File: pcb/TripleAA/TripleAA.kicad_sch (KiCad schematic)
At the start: 5 parts, among them U1 TPS564255

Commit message: Add components
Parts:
- removed U1: TPS564255, Package_TO_SOT_SMD:SOT-563, symbol Regulator_Switching_User:TPS564255
- added C5: 100nF,50V,X7R,0603, Capacitor_SMD:C_0603_1608Metric_Pad1.08x0.95mm_HandSolder, symbol Capacitor_User:100nF,50V,X7R,0603
- added C6: 56pF,50V,C0G,0603, Capacitor_SMD:C_0603_1608Metric_Pad1.08x0.95mm_HandSolder, symbol Capacitor_User:56pF,50V,C0G,0603
- added C7: 10uF,25V,X5R,0603, Capacitor_SMD:C_0603_1608Metric_Pad1.08x0.95mm_HandSolder, symbol Capacitor_User:10uF,25V,X5R,0603
- added J2: JST_S2B-PH-SM4-x, Connector_User:JST_PH_S2B-PH-SM4-TB_1x02-1MP_P2.00mm_Horizontal, symbol Connector_User:JST_S2B-PH-SM4-x
- added L1: 74438357068, Inductor_SMD_User:L_Wurth_WE-MAPI-4030, symbol Inductor_User:74438357068
- added R1: 20k,0603, Resistor_SMD:R_0603_1608Metric_Pad0.98x0.95mm_HandSolder, symbol Resistor_User:20k,0603
- added R2: 4.7k,0603, Resistor_SMD:R_0603_1608Metric_Pad0.98x0.95mm_HandSolder, symbol Resistor_User:4.7k,0603
- added U2: TPS562242, Package_TO_SOT_SMD:SOT-563, symbol Regulator_Switching_User:TPS562242
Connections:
- net +BATT: now reaches C3.1
- net +BATT: now also C2.1, C7.1, U2.1 (VIN), U2.5 (EN)
- net GND: now reaches C3.2
- net GND: now also C1.1, C2.2, C4.1, C6.1, J2.1 (Pin_1), L1.2, R1.1
- net -Vout: now reaches C4.2
- net -Vout: now also C1.2, C7.2, J2.2 (Pin_2), R2.2, U2.3 (GND)
- new net: C5.2, L1.1, U2.2 (SW)
- new net: C6.2, R1.2, R2.1, U2.6 (FB)
- new net: C5.1, U2.4 (BST)
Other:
- note added: "Battery Charger: BQ24040DSQR"
- moved on the sheet: C1, C2, C3, C4

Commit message: Update SCH and PCB
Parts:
- removed L1: 74438357068, Inductor_SMD_User:L_Wurth_WE-MAPI-4030, symbol Inductor_User:74438357068
- added C1, C2: 10uF,25V,X5R,0603, Capacitor_SMD:C_0603_1608Metric_Pad1.08x0.95mm_HandSolder, symbol Capacitor_User:10uF,25V,X5R,0603
- added D1: 824021, Package_TO_SOT_SMD_User:SOT-23_Handsoldering, symbol Power_Protection_User:824021
- added D2: 150080GS75000, LED_SMD:LED_0805_2012Metric_Pad1.15x1.40mm_HandSolder, symbol LED_User:150080GS75000
- added D3: 150080SS75000, LED_SMD:LED_0805_2012Metric_Pad1.15x1.40mm_HandSolder, symbol LED_User:150080SS75000
- added J1: JST_S2B-PH-SM4-x, Connector_User:JST_PH_S2B-PH-SM4-TB_1x02-1MP_P2.00mm_Horizontal, symbol Connector_User:JST_S2B-PH-SM4-x
- added unit 2 of J2
- added L1: 74438356056, Inductor_SMD_User:L_Wurth_WE-MAPI-4020, symbol Inductor_User:74438356056
- added R1, R2: 2k,0603, Resistor_SMD:R_0603_1608Metric_Pad0.98x0.95mm_HandSolder, symbol Resistor_User:2k,0603
- added R5: 27.4k,0603, Resistor_SMD:R_0603_1608Metric_Pad0.98x0.95mm_HandSolder, symbol Resistor_User:27.4k,0603
- added R6: 10k,0603, Resistor_SMD:R_0603_1608Metric_Pad0.98x0.95mm_HandSolder, symbol Resistor_User:10k,0603
- added U1: MCP73831-2-OT, Package_TO_SOT_SMD:SOT-23-5, symbol Battery_Management:MCP73831-2-OT
- added U3: BD4836G-xx, Package_TO_SOT_SMD:SOT-23-5, symbol Power_Supervisor_User:BD4836G-xx
- renumbered C2 to C4, C7 to C5, C5 to C6, C6 to C7, C1 to C8, C4 to C9, R1 to R3, R2 to R4
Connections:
- net +BATT: now also C2.1, R5.1, R6.1, U1.3 (V_{BAT}), U3.2 (VDD); no longer U2.5 (EN)
- net GND: now also C1.2, C2.2, D1.3 (A), J1.2 (Pin_2), J1.MP1 (MP), J1.MP2 (MP), J2.MP1 (MP), J2.MP2 (MP), L1.2, R2.2, U1.2 (V_{SS}), U3.3 (GND)
- net at C6.2, U2.2 (SW): now also L1.1
- new net: D3.1 (K), U3.1 (VOUT)
- new net: R1.2, U1.1 (STAT)
- new net: R2.1, U1.5 (PROG)
- new net: R6.2, U2.5 (EN)
- new net: D2.1 (K), R1.1
- new net: D3.2 (A), R5.2
- new net Vin: C1.1, D1.1 (K), D2.2 (A), J1.1 (Pin_1), U1.4 (V_{DD})
- no-connect marks 0 -> 1
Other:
- note added: "3.6 V threshold voltage"
- note added: "Ireg = 1 kV / R2 = 0.5 A"
- note added: "Low Battery Warning"
- note added: "Vout = 0.1 * (1 + R3 / R4) = 4.2 V"
- moved on the sheet: C3, C4, C5, C6, C7, C8, C9, R3, R4, U2

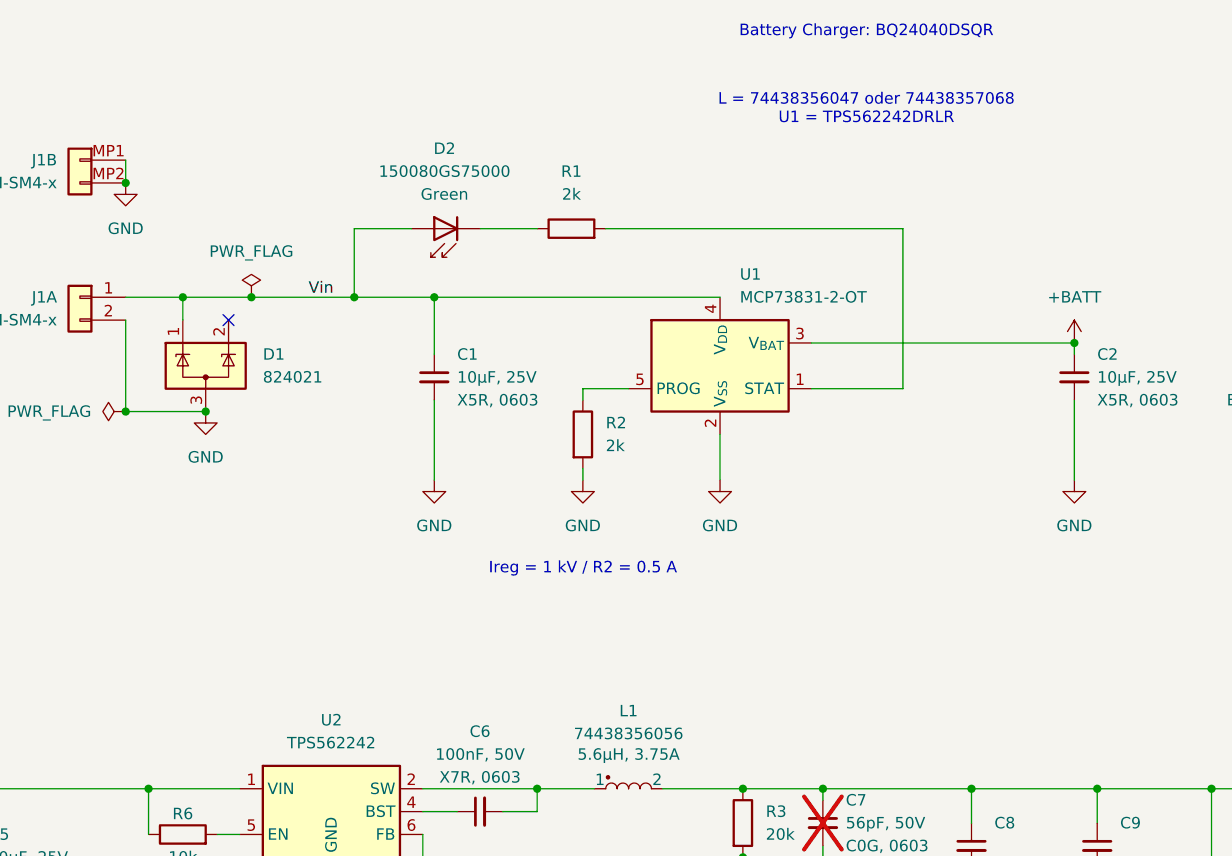
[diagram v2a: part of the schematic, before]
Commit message: Finalize PCB layout
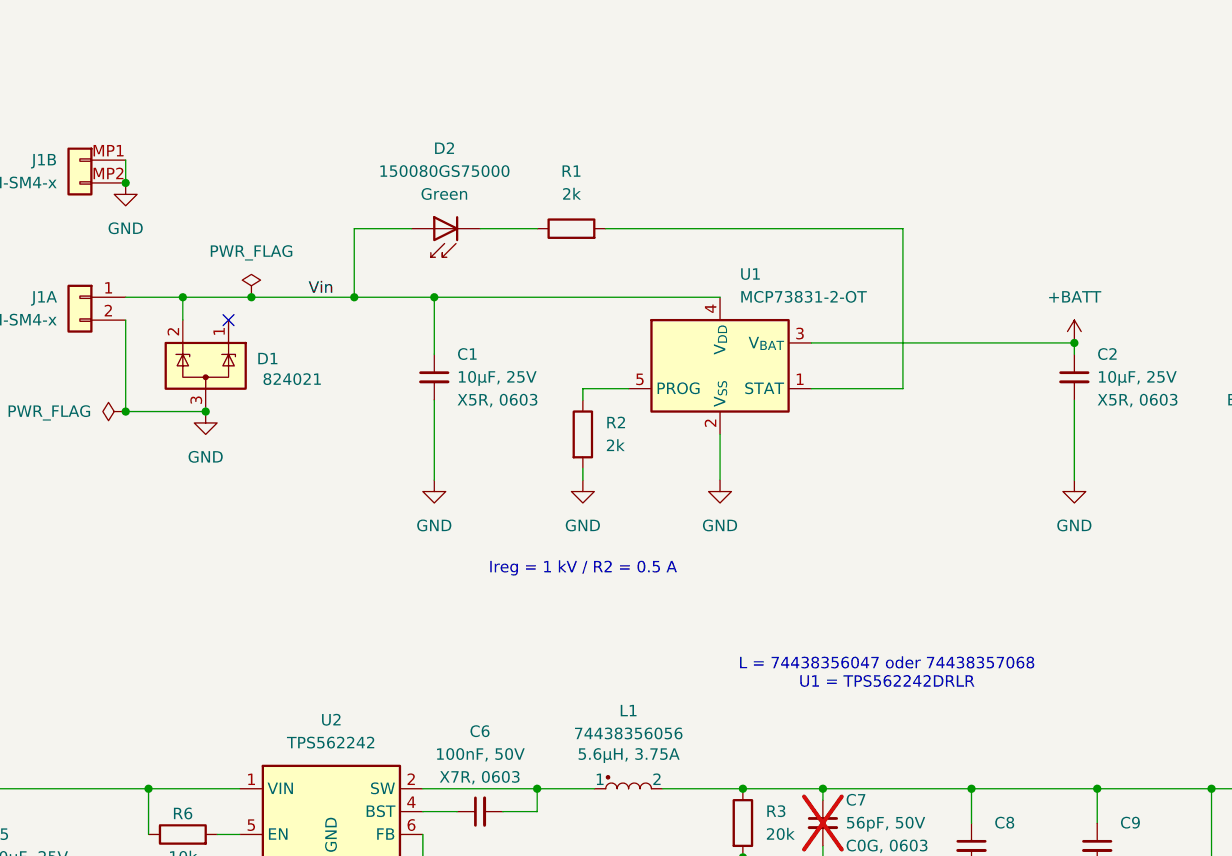
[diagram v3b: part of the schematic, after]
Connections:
- net Vin: now also D1.2 (K); no longer D1.1 (K)
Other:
- note removed: "Battery Charger: BQ24040DSQR"
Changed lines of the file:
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@@
-		)
-	)
-	(text "Battery Charger: BQ24040DSQR"
-		(exclude_from_sim no)
-		(at 169.926 28.956 0)
-		(effects
-			(font
-				(size 1.27 1.27)
-			)
 		)
 	)
@@
 	(text "L = 74438356047 oder 74438357068\nU1 = TPS562242DRLR"
 		(exclude_from_sim no)
-		(at 169.926 37.592 0)
+		(at 172.212 100.33 0)
 		(effects
 			(font
@@
 		(lib_id "Power_Protection_User:824021")
 		(at 96.52 66.04 0)
-		(unit 1)
-		(exclude_from_sim no)
-		(in_bom yes)
-		(on_board yes)
-		(dnp no)
-		(fields_autoplaced yes)
+		(mirror y)
+		(unit 1)
+		(exclude_from_sim no)
+		(in_bom yes)
+		(on_board yes)
+		(dnp no)
 		(property "Reference" "D1"
-			(at 102.87 64.7699 0)
+			(at 104.648 65.278 0)
 			(effects
 				(font
@@
 		)
 		(property "Value" "824021"
-			(at 102.87 67.3099 0)
+			(at 109.474 67.564 0)
 			(effects
 				(font
@@
 		)
 		(property "Footprint" "Package_TO_SOT_SMD_User:SOT-23_Handsoldering"
-			(at 102.235 67.31 0)
+			(at 90.805 67.31 0)
 			(effects
 				(font
@@
 		)
 		(property "Datasheet" "https://www.we-online.com/catalog/datasheet/824021.pdf"
-			(at 99.695 62.865 0)
+			(at 93.345 62.865 0)
 			(effects
 				(font
@@
 		)
 		(property "Manufacturer" "Wurth Elektronik"
-			(at 102.235 69.85 0)
+			(at 90.805 69.85 0)
 			(effects
 				(font
@@
 		)
 		(property "Supplier" "Digi-Key"
-			(at 102.235 72.39 0)
+			(at 90.805 72.39 0)
 			(effects
 				(font
@@
 		)
 		(property "SPN" "732-4468-1-ND"
-			(at 111.76 72.39 0)
-			(effects
-				(font
+			(at 81.28 72.39 0)
+			(effects
+				(font

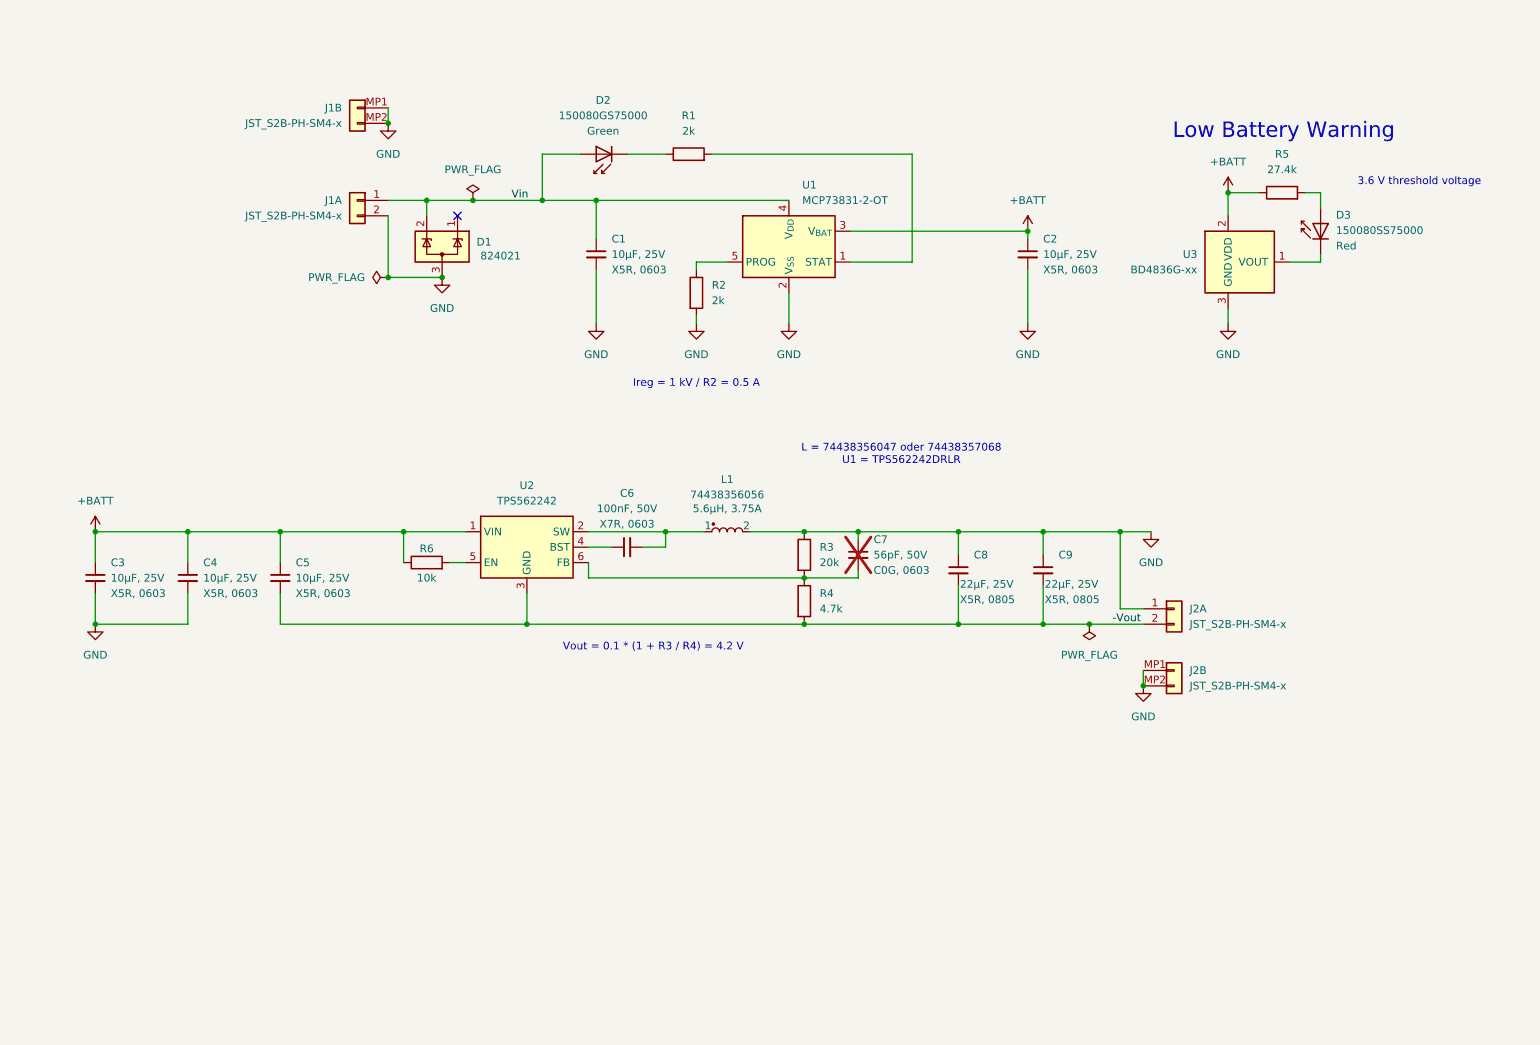
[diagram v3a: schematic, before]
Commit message: Add USB connector
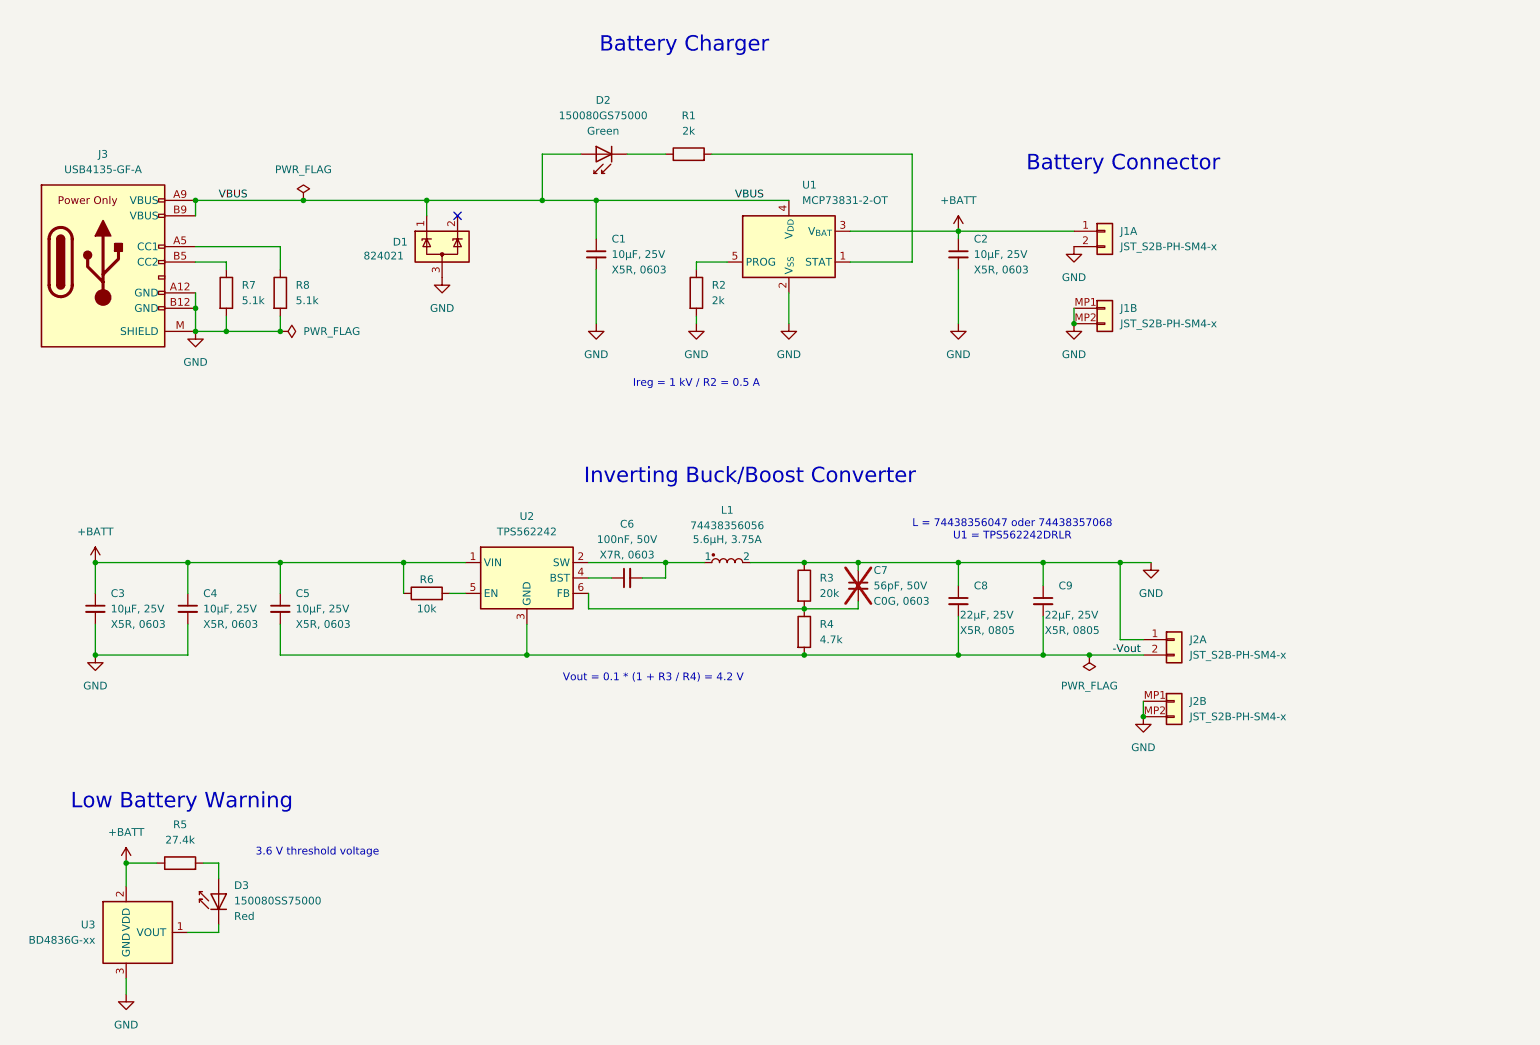
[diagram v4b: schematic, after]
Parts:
- added J3: USB4135-GF-A, Connector_User:USB-C_Receptacle_GTC_USB4135-GF-A, symbol Connector_User:USB4135-GF-A
- added R7, R8: 5.1k,0603, Resistor_SMD:R_0603_1608Metric_Pad0.98x0.95mm_HandSolder, symbol Resistor_User:5.1k,0603
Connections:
- net +BATT: now also J1.1 (Pin_1)
- net GND: now also J3.A12 (GND), J3.B12 (GND), J3.M (SHIELD), R7.2, R8.2
- net VBUS: now reaches D1.1 (K)
- net VBUS: now also C1.1, D2.2 (A), U1.4 (V_{DD}), J3.A9 (VBUS), J3.B9 (VBUS)
- removed net Vin: C1.1, D1.2 (K), D2.2 (A), J1.1 (Pin_1), U1.4 (V_{DD})
- new net: J3.A5 (CC1), R8.1
- new net: J3.B5 (CC2), R7.1
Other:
- note added: "Battery Charger"
- note added: "Battery Connector"
- note added: "Inverting Buck/Boost Converter"
- moved on the sheet: C2, C3, C4, C5, C6, C7, C8, C9, D3, J1A, J1B, J2A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

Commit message: RevA
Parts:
- L1: value 74438356056 -> SRN4018-4R7M; footprint Inductor_SMD_User:L_Wurth_WE-MAPI-4020 -> Inductor_SMD:L_Bourns-SRN4018; symbol Inductor_User:74438356056 -> Inductor_User:SRN4018-4R7M; MPN 74438357068 -> SRN4018-4R7M; Manufacturer Wurth Electronics -> Bourns; Pretty Value 1 5.6µH, 3.75A -> 4.7µH, 2A; SPN 732-8235-1-ND -> BOU SRN4018-4R7M; Supplier Digi-Key -> Reichelt
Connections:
- net VBUS: now also D1.2 (K)
- no-connect marks 1 -> 0
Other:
- company: (none) -> fl0m0
- title: (none) -> AA Battery Pack Replacement
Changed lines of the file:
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@@
 	(generator_version "8.0")
 	(paper "A4")
+	(title_block
+		(title "AA Battery Pack Replacement")
+		(date "2024-12-01")
+		(rev "A")
+		(company "fl0m0")
+	)
 	(junction
 		(at 69.85 80.01)
@@
 	)
 	(junction
+		(at 99.06 58.42)
+		(diameter 0)
+		(color 0 0 0 0)
+	)
+	(junction
 		(at 156.21 118.11)
 		(diameter 0)
@@
 		(color 0 0 0 0)
 	)
-	(no_connect
-		(at 99.06 60.96)
-	)
 	(wire
 		(pts
@@
 	(wire
 		(pts
-			(xy 93.98 58.42) (xy 113.03 58.42)
+			(xy 93.98 58.42) (xy 99.06 58.42)
 		)
 		(stroke
@@
 	(wire
 		(pts
+			(xy 99.06 58.42) (xy 99.06 60.96)
+		)
+		(stroke
+			(width 0)
+			(type default)
+		)
+	)
+	(wire
+		(pts
 			(xy 127 50.8) (xy 133.35 50.8)
 		)
@@
 		(pts
 			(xy 54.61 179.07) (xy 59.69 179.07)
+		)
+		(stroke
+			(width 0)
+			(type default)
+		)
+	)
+	(wire
+		(pts
+			(xy 99.06 58.42) (xy 113.03 58.42)
 		)
 		(stroke
@@
 	)
 	(symbol
-		(lib_id "Inductor_User:74438356056")
+		(lib_id "Inductor_User:SRN4018-4R7M")
 		(at 143.51 118.11 90)
 		(unit 1)
@@
 		(dnp no)
 		(property "Reference" "L1"
-			(at 143.51 109.474 90)
-			(effects
-				(font
-					(size 1.27 1.27)
-				)
-			)
-		)
-		(property "Value" "74438356056"
-			(at 143.51 112.014 90)
-			(effects
-				(font
-					(size 1.27 1.27)
-				)
-			)
-		)
-		(property "Footprint" "Inductor_SMD_User:L_Wurth_WE-MAPI-4020"
+			(at 143.51 112.268 90)
+			(effects
+				(font
+					(size 1.27 1.27)
+				)
+			)
+		)
+		(property "Value" "SRN4018-4R7M"
+			(at 143.51 114.554 90)
+			(effects
+				(font
+					(size 1.27 1.27)
+				)
+			)
+		)
+		(property "Footprint" "Inductor_SMD:L_Bourns-SRN4018"
 			(at 142.24 119.888 90)
 			(effects
@@
 			)
 		)
-		(property "Datasheet" "https://www.we-online.com/components/products/datasheet/74438357068.pdf"
+		(property "Datasheet" "https://www.bourns.com/docs/product-datasheets/srn4018.pdf?sfvrsn=528a0331_24"
 			(at 156.21 107.95 0)
 			(effects
@@
 			)
 		)
-		(property "Description" "WE-MAPI SMT Shielded Power Inductor, 5.6µH, 3.85A, 81mΩ"
+		(property "Description" "Semi Shielded Power Inductor, 4.7µH, 2A, 84mΩ"
 			(at 143.51 118.11 0)
 			(effects
@@
 			)
 		)
-		(property "Manufacturer" "Wurth Electronics"
+		(property "Manufacturer" "Bourns"
 			(at 163.83 116.84 0)
 			(effects
@@
 			)
 		)
-		(property "MPN" "74438357068"
-			(at 143.51 111.76 90)
-			(effects
-				(font
-					(size 1.27 1.27)
-				)
-				(hide yes)
-			)
-		)
-		(property "Pretty Value 1" "5.6µH, 3.75A"
-			(at 143.51 114.3 90)
-			(effects
-				(font
-					(size 1.27 1.27)
-				)
-			)
-		)
-		(property "Supplier" "Digi-Key"
+		(property "MPN" "SRN4018-4R7M"
+			(at 143.51 118.11 0)
+			(effects
+				(font
+					(size 1.27 1.27)
+				)
+				(hide yes)
+			)
+		)
+		(property "Pretty Value 1" "4.7µH, 2A"
+			(at 143.51 120.142 90)
+			(effects
+				(font
+					(size 1.27 1.27)
+				)
+			)
+		)
+		(property "Supplier" "Reichelt"
 			(at 160.02 130.81 0)
 			(effects
@@
 			)
 		)
-		(property "SPN" "732-8235-1-ND"
+		(property "SPN" "BOU SRN4018-4R7M"
 			(at 160.02 116.84 0)
 			(effects
